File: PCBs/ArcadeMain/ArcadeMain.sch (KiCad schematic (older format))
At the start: 8 parts, among them J1 Conn_01x17_Male, J2 Conn_01x17_Male, J21 USB_B_Micro, J23 Conn_02x22_Top_Bottom, J24 USB_B_Micro, J3 Screw_Terminal_01x12, J4 Conn_01x17_Male, J5 Conn_01x17_Male

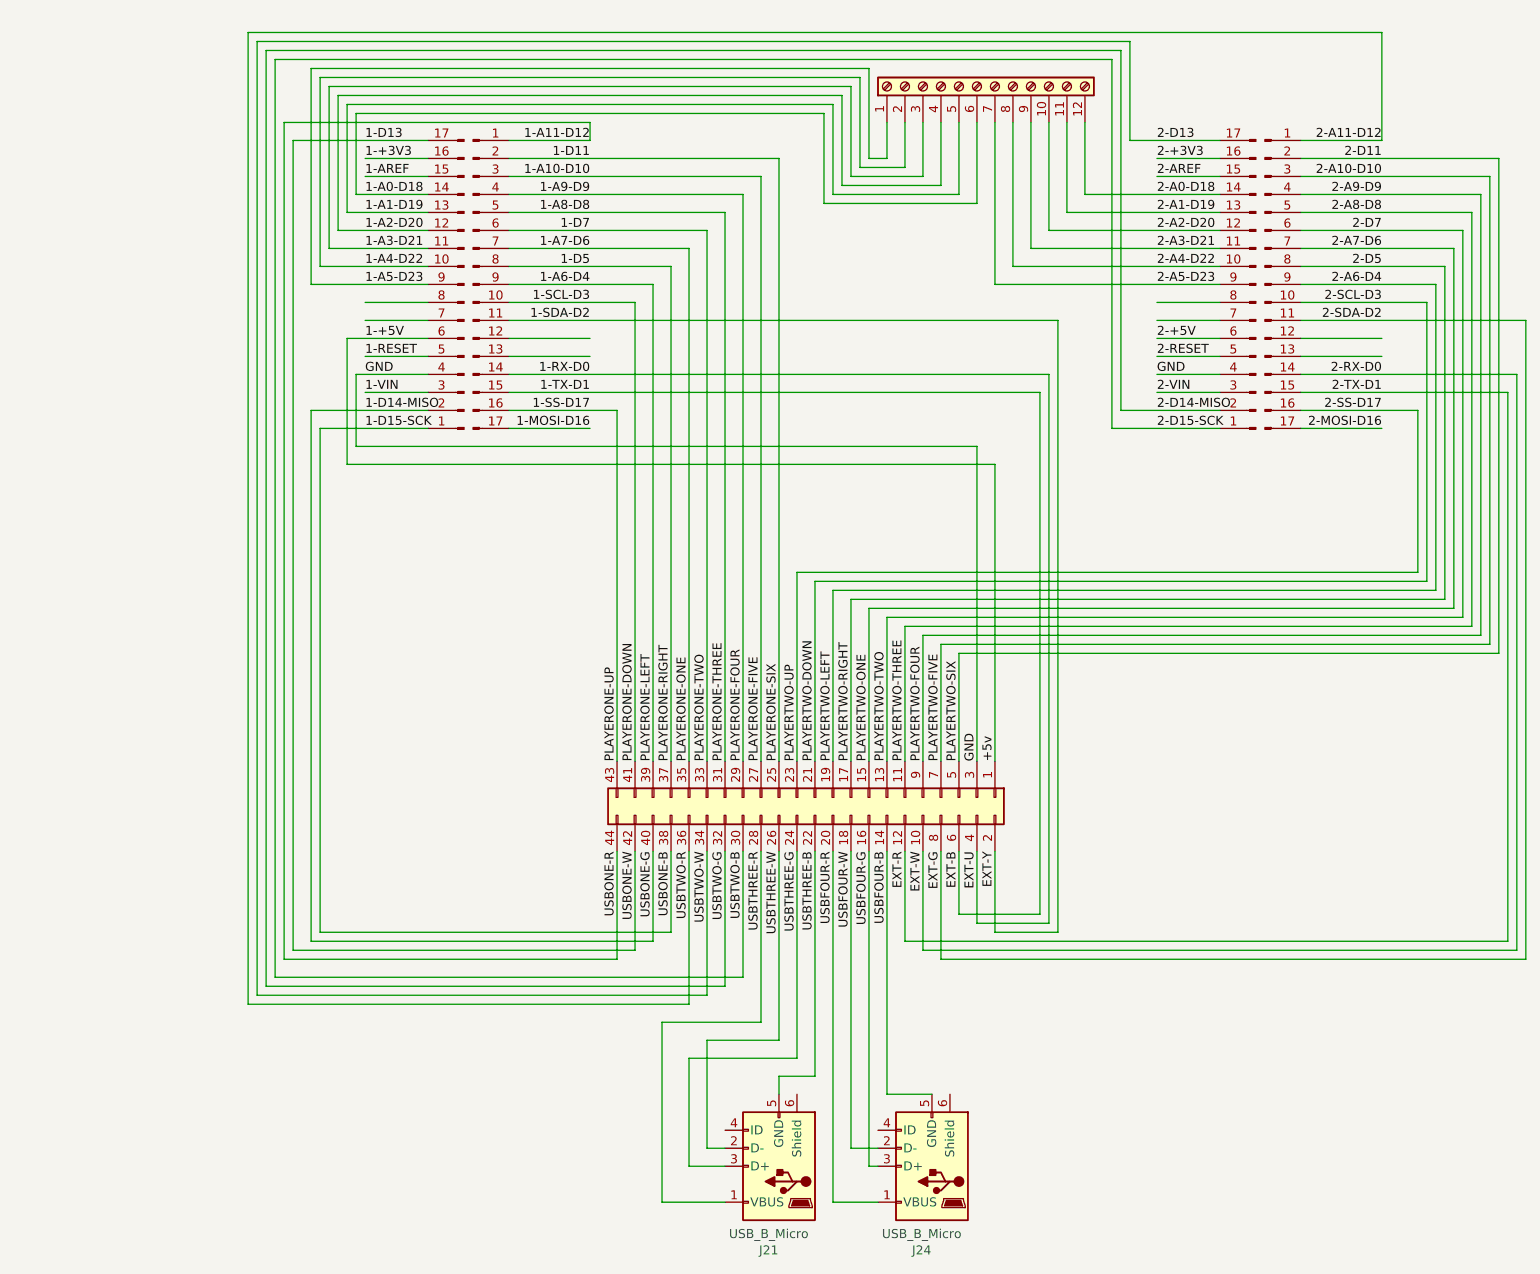
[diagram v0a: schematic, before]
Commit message: v2 PCB revisions: switch to ribbon cable rather than PCB edge, add DIP switch for panel identifications
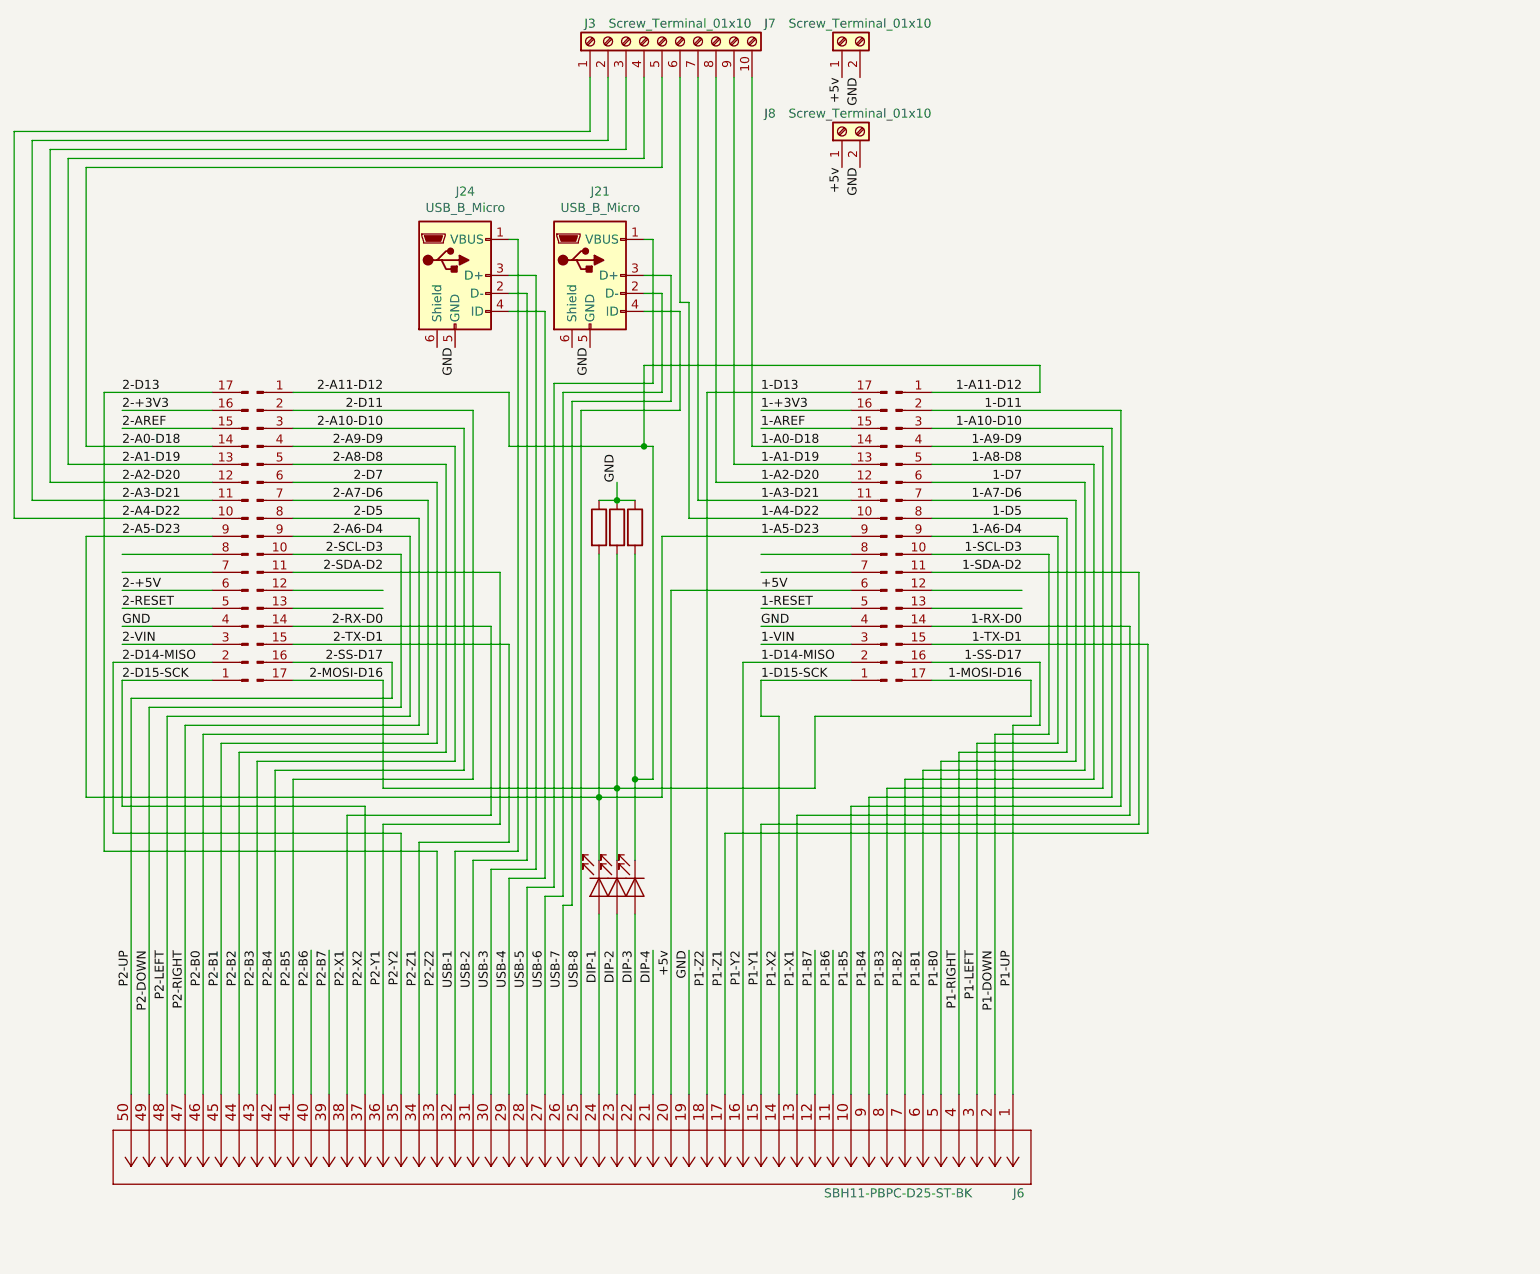
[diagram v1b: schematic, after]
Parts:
- removed J23: Conn_02x22_Top_Bottom, Connector_PinHeader_2.54mm:PinHeader_2x22_P2.54mm_Horizontal, symbol Connector_Generic:Conn_02x22_Odd_Even
- removed J3: Screw_Terminal_01x12, TB001-500-12BE:CUI_TB001-500-12BE, symbol Connector:Screw_Terminal_01x12
- added D1, D2, D3: LED, LED_THT:LED_D3.0mm, symbol Device:LED
- added J3: Screw_Terminal_01x10, TB001-500-10BE:CUI_TB001-500-10BE, symbol Connector:Screw_Terminal_01x10
- added J6: SBH11-PBPC-D25-ST-BK, ul_SBH11PBPCD25STBK:SBH11-PBPC-D25-ST-BK, symbol 2020-07-14_18-22-10:SBH11-PBPC-D25-ST-BK
- added J7, J8: Screw_Terminal_01x10, TB001-500-08BE:CUI_TB001-500-02BE, symbol Connector:Screw_Terminal_01x02
- added R1, R2, R3: 220, Resistor_THT:R_Axial_DIN0204_L3.6mm_D1.6mm_P7.62mm_Horizontal, symbol Device:R
- J21, J24: footprint digikey-footprints:USB_Micro_B_Female_10118194-0001LF -> ryan-common-library:GCT_USB3131-XX-0230-X_REVB
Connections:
- net labels added: +5V, DIP-1, DIP-2, DIP-3, DIP-4, P1-B0, P1-B1, P1-B2, P1-B3, P1-B4, P1-B5, P1-B6, P1-B7, P1-DOWN, P1-LEFT, P1-RIGHT, P1-UP, P1-X1, P1-X2, P1-Y1, P1-Y2, P1-Z1, P1-Z2, P2-B0, P2-B1, P2-B2, P2-B3, P2-B4, P2-B5, P2-B6, P2-B7, P2-DOWN, P2-LEFT, P2-RIGHT, P2-UP, P2-X1, P2-X2, P2-Y1, P2-Y2, P2-Z1, P2-Z2, USB-1, USB-2, USB-3, USB-4, USB-5, USB-6, USB-7, USB-8
- net labels removed: 1-+5V, EXT-B, EXT-G, EXT-R, EXT-U, EXT-W, EXT-Y, PLAYERONE-DOWN, PLAYERONE-FIVE, PLAYERONE-FOUR, PLAYERONE-LEFT, PLAYERONE-ONE, PLAYERONE-RIGHT, PLAYERONE-SIX, PLAYERONE-THREE, PLAYERONE-TWO, PLAYERONE-UP, PLAYERTWO-DOWN, PLAYERTWO-FIVE, PLAYERTWO-FOUR, PLAYERTWO-LEFT, PLAYERTWO-ONE, PLAYERTWO-RIGHT, PLAYERTWO-SIX, PLAYERTWO-THREE, PLAYERTWO-TWO, PLAYERTWO-UP, USBFOUR-B, USBFOUR-G, USBFOUR-R, USBFOUR-W, USBONE-B, USBONE-G, USBONE-R, USBONE-W, USBTHREE-B, USBTHREE-G, USBTHREE-R, USBTHREE-W, USBTWO-B, USBTWO-G, USBTWO-R, USBTWO-W
- wire segments 225 -> 257
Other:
- moved on the sheet: J21, J24
